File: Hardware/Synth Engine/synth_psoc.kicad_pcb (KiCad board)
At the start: 2 copper layers, 124.5 x 129.5 mm, 238 parts, among them J1 Barrel_Jack, J10 USB_C_Receptacle, J13 Conn_01x05, J14 Conn_01x05, J15 Conn_01x05, J16 Conn_01x05, J2 Audio-Jack-2_Switch, J3 SWD_programming, J4 Conn_01x08, J5 Conn_01x08, J6 Conn_01x03, J7 Capsense_buttons, J8 Conn_02x13_Odd_Even, J9 Conn_02x13_Odd_Even, Q1 MMBT3904-TP, Q2 MMBT3904-TP, Q3 MMBT3904-TP, Q4 MMBT3904-TP, Q5 MMBFJ177, Q6 MMBFJ177, Q7 MMBFJ177, Q8 MMBFJ177, U1 TL074, U2 TL074, U3 TL074, U4 TL074, U5 TL074, U6 CY8C4246AZI-L445, U7 V7805-1000, U8 PT2399, Y1 16MHz, Y2 32.768kHz

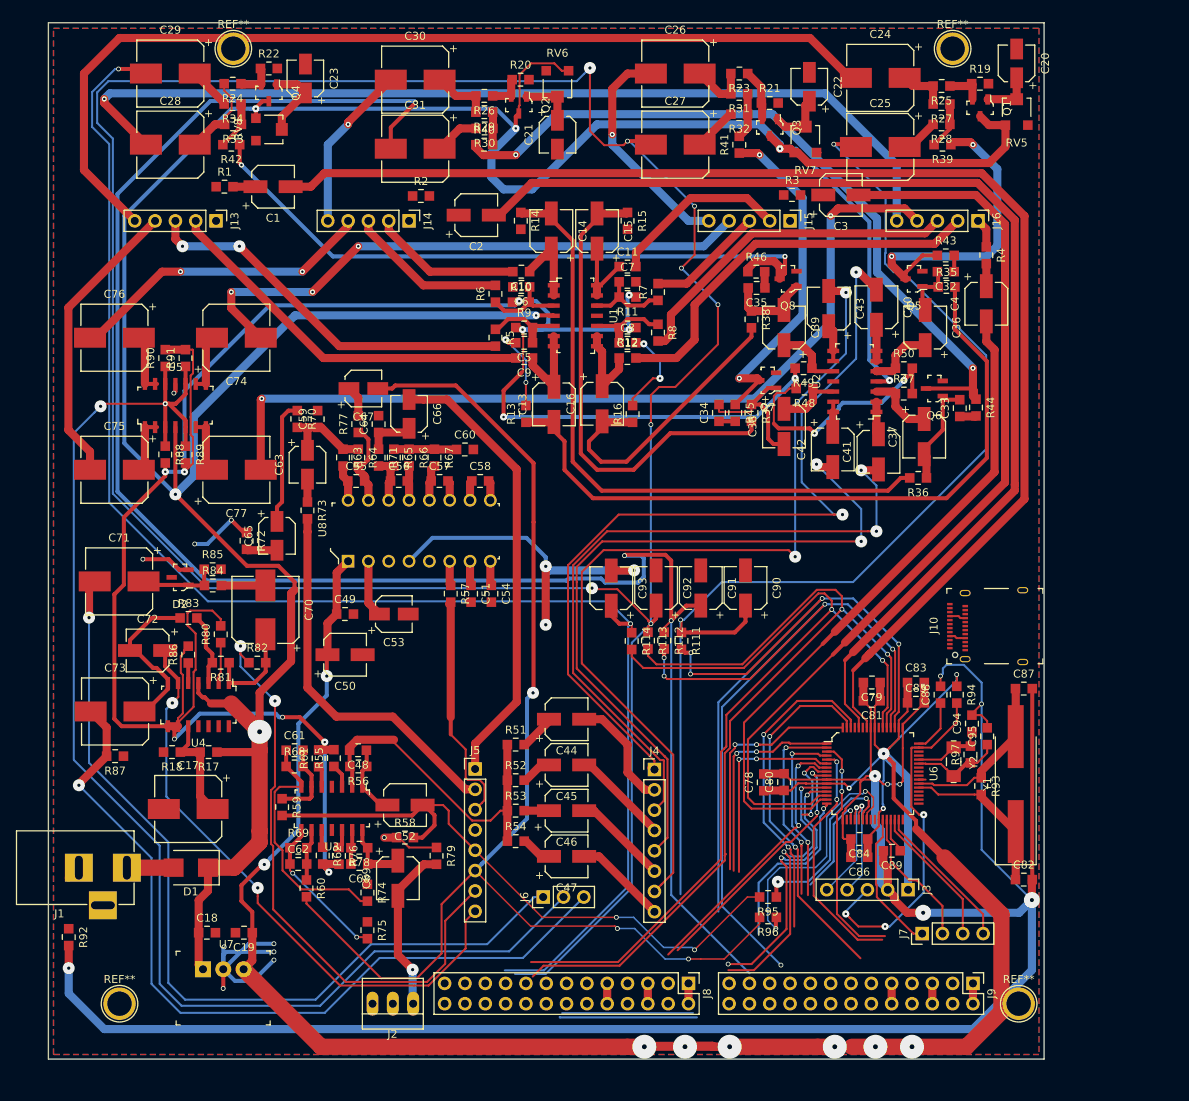
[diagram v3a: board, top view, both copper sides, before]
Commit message: reroute first connector on main board
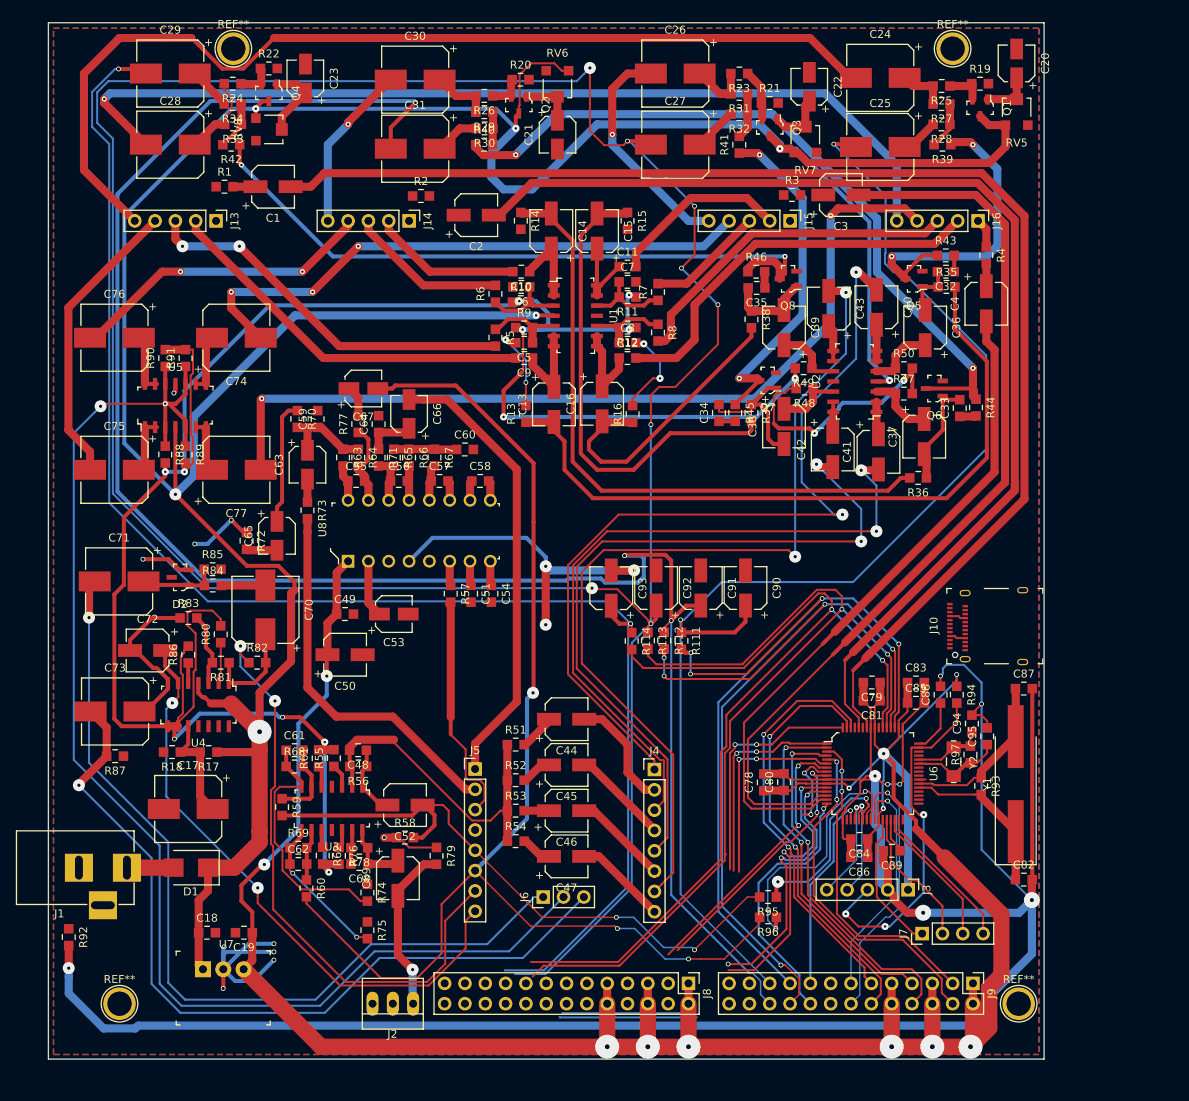
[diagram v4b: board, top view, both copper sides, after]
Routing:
- net +5V: track 368.8 -> 333.6 mm
- net /Connectors/osc2_quant: track 0.00 -> 34.6 mm, vias 0 -> 1
- net /Connectors/osc1_quant: track 0.00 -> 29.4 mm, vias 0 -> 1
- net /Connectors/osc2_pwm_wiper: track 22.9 -> 45.0 mm
- net /Connectors/osc1_pwm_wiper: track 24.4 -> 42.9 mm
- net /Microcontroller/envelope_pwm_1: track 145.3 -> 161.1 mm
- net /Connectors/osc2_freq_wiper: track 30.1 -> 43.3 mm
- net /Connectors/envelope_pwm_bypass_in_1: track 91.6 -> 104.2 mm
- net /Connectors/osc1_repeat: track 12.7 -> 25.0 mm
- net /Connectors/osc2_repeat: track 21.9 -> 33.3 mm
- net /Connectors/osc1_speed: track 40.2 -> 51.3 mm
- net /Connectors/osc1_freq_wiper: track 29.0 -> 39.9 mm
- net /Connectors/osc2_speed: track 45.2 -> 52.7 mm
- net /Connectors/envelope_pwm_bypass_in_2: track 102.0 -> 108.5 mm
- net /Microcontroller/envelope_pwm_2: track 230.4 -> 235.5 mm
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
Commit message: redo second connector on main board
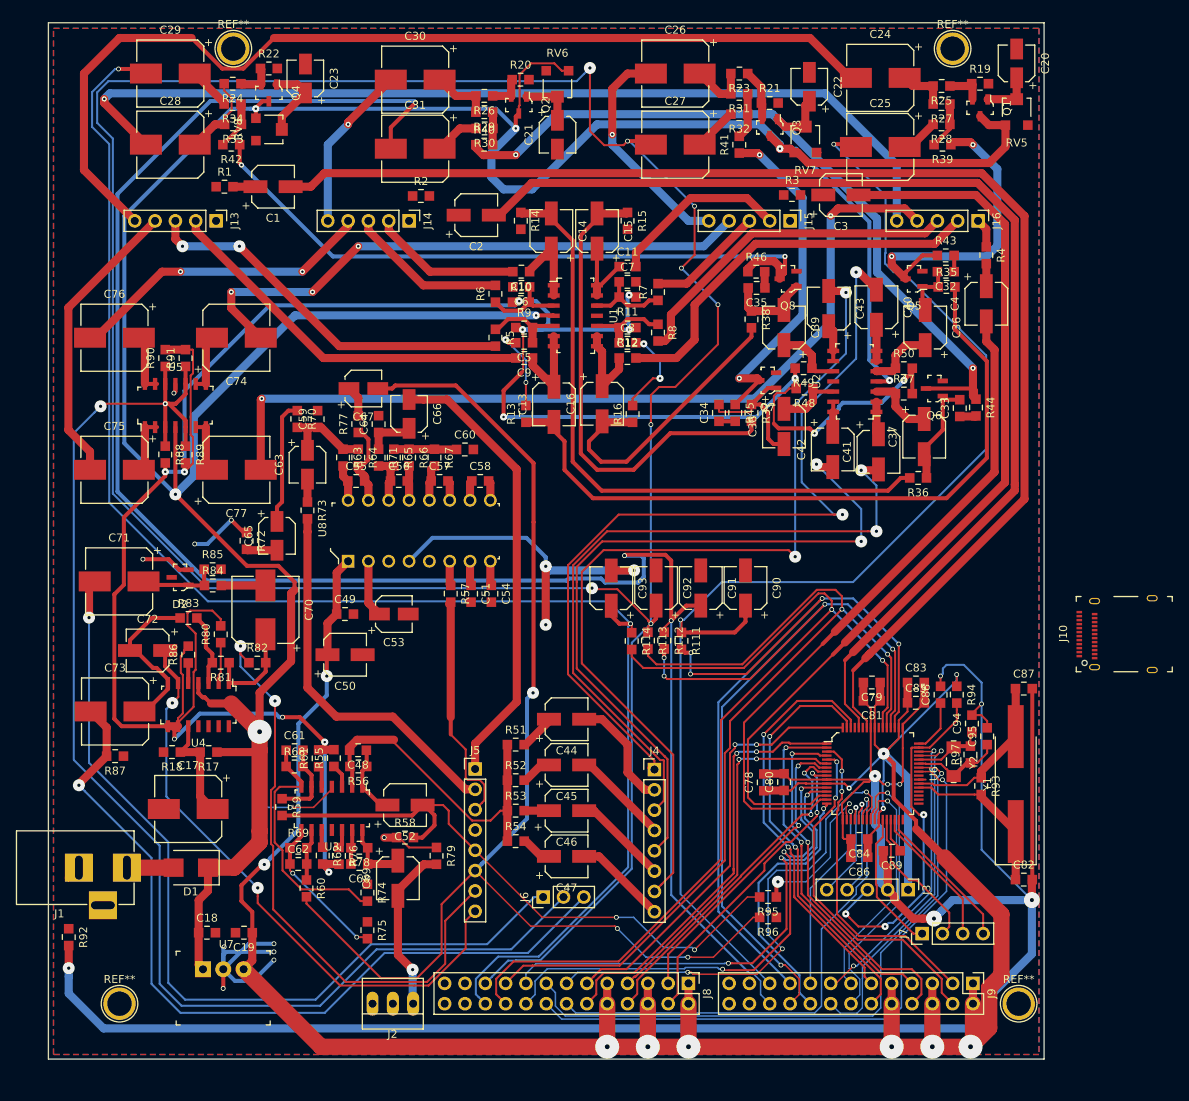
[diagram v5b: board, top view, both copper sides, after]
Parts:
- moved J10 16.2 mm to (149.8, 98.6)
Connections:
- U6 pad 41: /Microcontroller/osc4_hold -> /Connectors/osc4_hold
- U6 pad 42: /Microcontroller/osc3_hold -> /Connectors/osc3_hold
- U6 pad 45: /Microcontroller/osc2_hold -> /Connectors/osc2_hold
- U6 pad 46: /Microcontroller/osc1_hold -> /Connectors/osc1_hold
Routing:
- net /Connectors/osc3_hold: track 0.00 -> 80.5 mm, vias 0 -> 1
- net /Connectors/osc4_hold: track 0.00 -> 80.2 mm, vias 0 -> 1
- net /Connectors/osc3_quant: track 10.5 -> 61.7 mm, vias 1 -> 3
- net /Connectors/osc2_hold: track 0.00 -> 44.0 mm, vias 0 -> 1
- net /Connectors/osc4_quant: track 20.3 -> 63.9 mm
- net /Connectors/osc1_hold: track 0.00 -> 37.0 mm, vias 0 -> 2
- net (no net): track 33.6 -> 0.00 mm
- net /Connectors/osc4_pwm_wiper: track 10.1 -> 42.8 mm
- net /Connectors/osc4_repeat: track 35.6 -> 63.9 mm, vias 2 -> 3
- net /Connectors/osc3_repeat: track 33.5 -> 60.4 mm
- net /Connectors/osc4_speed: track 27.0 -> 53.7 mm
- net /Connectors/osc3_speed: track 30.2 -> 53.7 mm
- net /mcu_delay_out: track 21.5 -> 0.10 mm, vias 1 -> 0
- net /Connectors/osc3_pwm_wiper: track 25.3 -> 45.1 mm
- net +15V: track 408.0 -> 427.2 mm, vias 7 -> 8
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
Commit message: fix some missing traces on main board
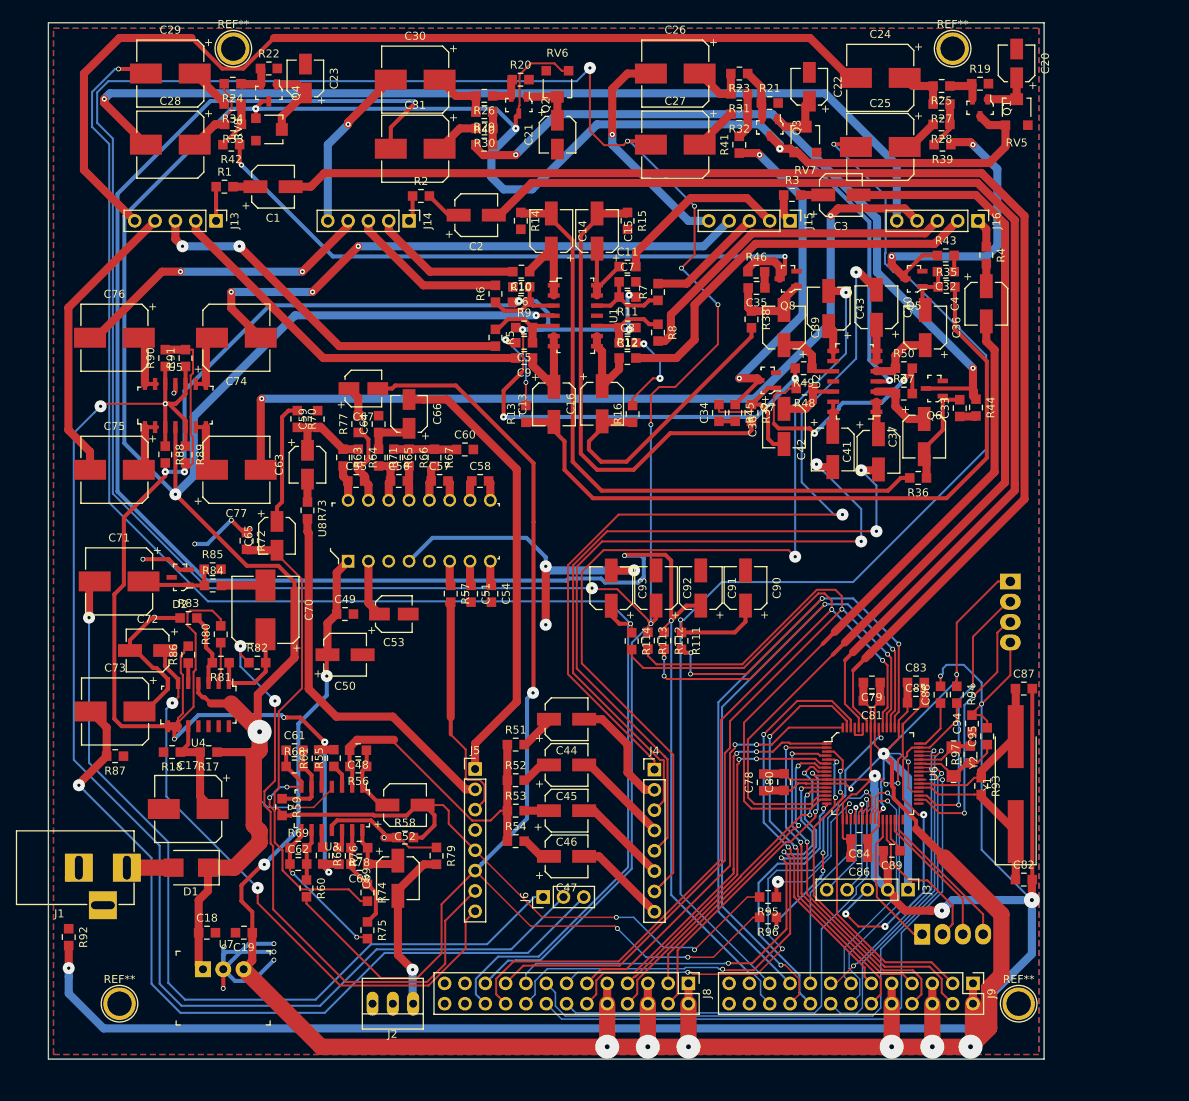
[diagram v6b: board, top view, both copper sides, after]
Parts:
- J10: value USB_C_Receptacle -> USB; footprint digikey-footprints:USB_Type_C_Female__12401610E4_2A -> Connectors_Molex:Molex_KK-6410-04_04x2.54mm_Straight; moved to B.Cu
- J7: footprint Pin_Headers:Pin_Header_Straight_1x04_Pitch2.54mm -> Connectors_Molex:Molex_KK-6410-04_04x2.54mm_Straight; moved to B.Cu
- moved J10 12.4 mm to (139.3, 92.0), turned to 270 degrees
- moved J7 0.08 mm to (128.3, 136.1), turned to 0 degrees
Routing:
- net /Mixer and Effects/delay_in: track 81.8 -> 118.2 mm
- net /Microcontroller/USB_D_n: track 0.00 -> 33.7 mm, vias 0 -> 2
- net /Microcontroller/USB_D_p: track 0.00 -> 32.8 mm, vias 0 -> 2
- net /mcu_delay_out: track 0.10 -> 32.1 mm, vias 0 -> 4
- net +5V: track 329.5 -> 353.6 mm, vias 12 -> 13
- net Net-(C68-Pad2): track 4.32 -> 13.3 mm
- net GND: track 119.8 -> 128.4 mm
- net GNDD: track 308.4 -> 316.5 mm
- net Net-(C2-Pad1): track 0.00 -> 4.65 mm
- net /Connectors/freq_in_1: track 0.06 -> 4.34 mm
- net /Connectors/freq_in_3: track 0.00 -> 3.57 mm
- net /Connectors/freq_in_2: track 0.00 -> 3.29 mm
- net Net-(C3-Pad1): track 0.00 -> 2.85 mm
- net Net-(U6-Pad59): track 0.00 -> 2.77 mm
- net Net-(J7-Pad2): track 18.4 -> 19.6 mm
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
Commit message: new release candidate. Passes DRC.
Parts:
- J1: value Barrel_Jack -> Conn_01x02; footprint Connectors:BARREL_JACK -> Connectors_Molex:Molex_KK-6410-02_02x2.54mm_Straight
- J2: footprint Connectors:PINHEAD1-3 -> Connectors_Molex:Molex_KK-6410-03_03x2.54mm_Straight
- moved J1 6.02 mm to (22.9, 128.3), turned to 270 degrees
- moved J2 0.06 mm to (64.6, 144.7)
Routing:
- net GND: track 128.4 -> 490.2 mm, vias 17 -> 61
- net Net-(D1-Pad2): track 5.84 -> 12.0 mm
- net Net-(U6-Pad39): track 0.89 -> 0.03 mm
- net /LFO Modulation and Routing/lfo_tri: track 102.3 -> 101.6 mm

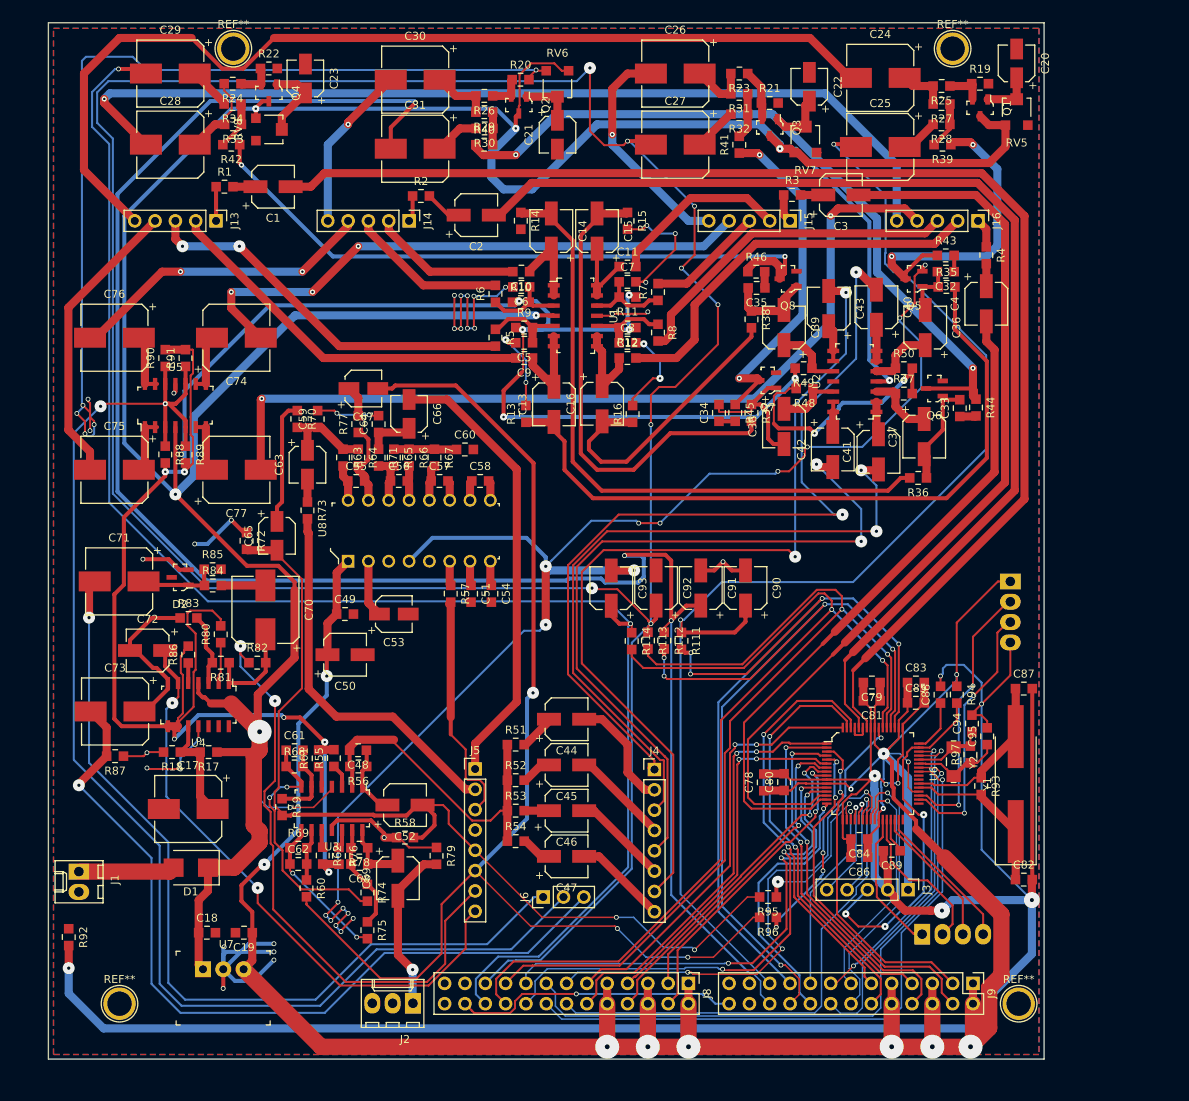
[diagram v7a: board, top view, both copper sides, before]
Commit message: add MIDI
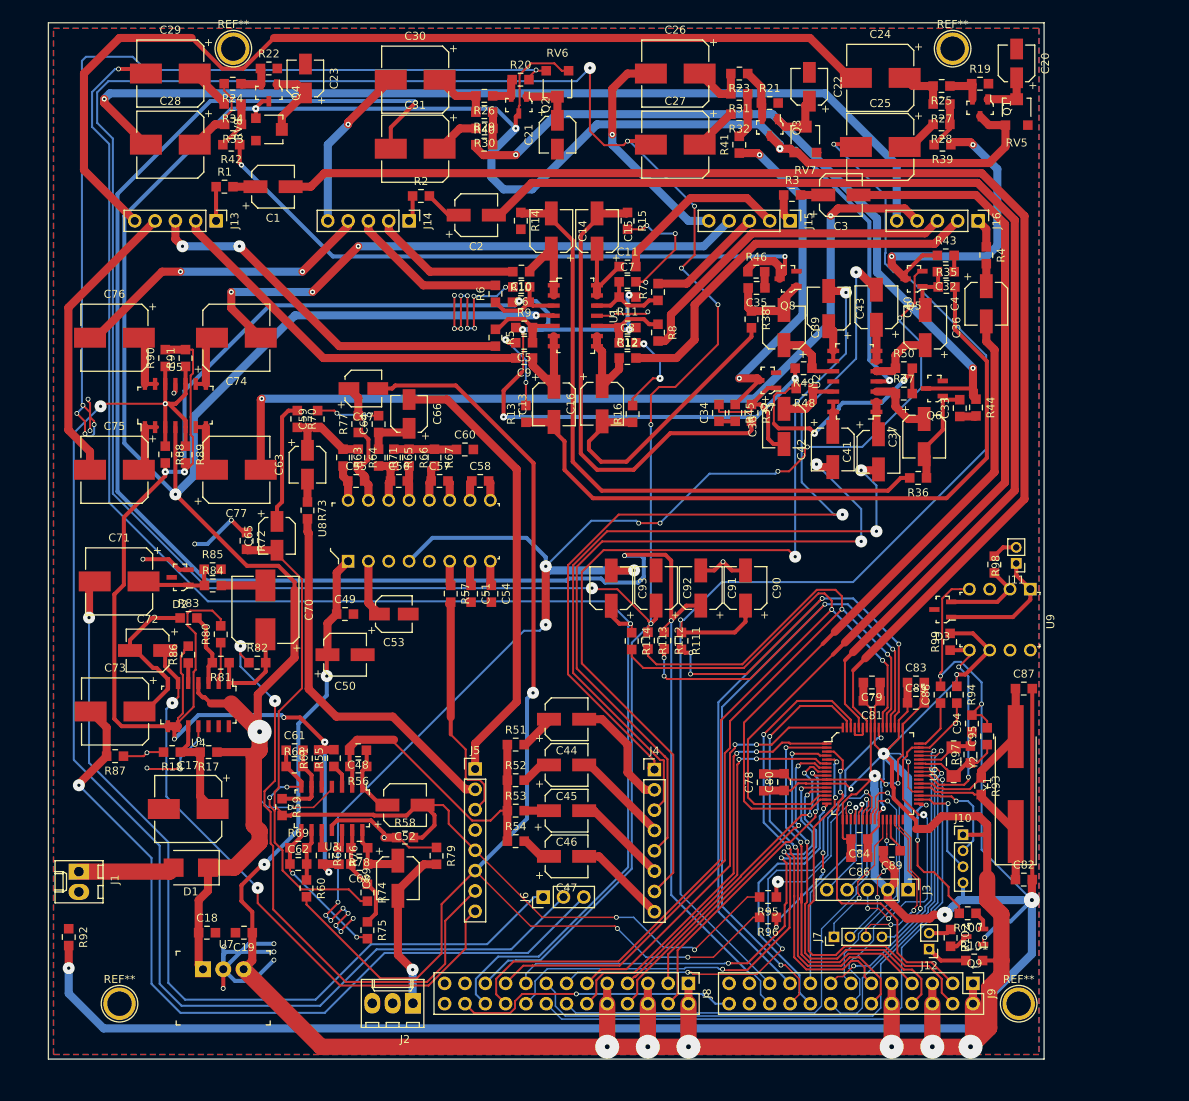
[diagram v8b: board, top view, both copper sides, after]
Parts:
- added D3: D, digikey-footprints:SOT-23-3, F.Cu at (130.8, 95.5)
- added J11: MIDI IN, Pin_Headers:Pin_Header_Straight_1x02_Pitch2.00mm, F.Cu at (140.0, 89.7)
- added J12: MIDI OUT, Pin_Headers:Pin_Header_Straight_1x02_Pitch2.00mm, F.Cu at (129.1, 138.0)
- added Q9: 2N3904, digikey-footprints:SOT-23-3, F.Cu at (134.8, 136.4)
- added R100: 10k, digikey-footprints:0805, F.Cu at (134.0, 133.5)
- added R101: 220, digikey-footprints:0805, F.Cu at (134.8, 139.4)
- added R102: 220, digikey-footprints:0805, F.Cu at (131.8, 136.6)
- added R98: 220, digikey-footprints:0805, F.Cu at (137.3, 89.9)
- added R99: 280, digikey-footprints:0805, F.Cu at (131.8, 99.5)
- added U9: 4N28, digikey-footprints:DIP-8_W7.62mm, F.Cu at (141.8, 93.0)
- J10, J7: footprint Connectors_Molex:Molex_KK-6410-04_04x2.54mm_Straight -> Pin_Headers:Pin_Header_Straight_1x04_Pitch2.00mm; moved to F.Cu
- moved J10 32.2 mm to (133.4, 123.7), turned to 0 degrees
- moved J7 11.0 mm to (117.2, 136.4), turned to 90 degrees
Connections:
- U6 pad 33: Net-(U6-Pad33) -> /Microcontroller/MIDI_OUT
- U6 pad 40: Net-(U6-Pad40) -> /Microcontroller/MIDI_IN
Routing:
- net /Microcontroller/MIDI_IN: track 0.00 -> 26.7 mm, vias 0 -> 2
- net /Microcontroller/USB_D_n: track 33.7 -> 13.4 mm, vias 2 -> 1
- net /Microcontroller/USB_D_p: track 32.8 -> 12.7 mm, vias 2 -> 1
- net /Microcontroller/MIDI_OUT: track 0.00 -> 18.1 mm, vias 0 -> 2
- net GNDD: track 316.5 -> 333.9 mm, vias 8 -> 9
- net Net-(D3-Pad1): track 0.00 -> 16.1 mm
- net Net-(D3-Pad2): track 0.00 -> 10.9 mm
- net +5V: track 353.6 -> 362.0 mm
- net /Connectors/osc1_pwm_wiper: track 42.6 -> 49.1 mm
- net /Connectors/osc2_freq_wiper: track 43.4 -> 49.2 mm
- net /Connectors/osc2_pwm_wiper: track 45.0 -> 50.6 mm
- net /Connectors/osc2_speed: track 52.4 -> 57.7 mm
- net /Connectors/osc1_speed: track 51.3 -> 56.6 mm
- net Net-(J12-Pad1): track 0.00 -> 5.17 mm
- net /Microcontroller/XRES: track 45.5 -> 41.6 mm
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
